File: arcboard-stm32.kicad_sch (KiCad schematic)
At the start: 85 parts, among them J10 Conn_01x04_Socket, J13 FFC05001-12SBA124W5M, J14 FFC05001-12SBA124W5M, J15 FFC05001-12SBA124W5M, J16 FFC05001-12SBA124W5M, J2 Conn_01x04_Socket, J3 FFC05001-12SBA124W5M, J4 FFC05001-12SBA124W5M, J5 Conn_01x02_Socket, J6 FFC05001-12SBA124W5M, J7 FFC05001-12SBA124W5M, J8 FFC05001-12SBA124W5M, J9 Conn_01x03_Socket, U1 XC6210B332MR-G, U10 1N4148W_C81598, U11 W25Q16JVSSIQTR, U12 TYPE-C-31-M-13, U13 2N7002, U15 TS-1187A-B-A-B, U2 TYPE-C-31-M-13, U3 STM32F405RGTx, U4 2N7002, U5 BAV70S,115, U6 BAV70S,115, U7 BAV70S,115, U8 BAV70S,115, U9 BAV70S,115, Y1 Crystal_GND24

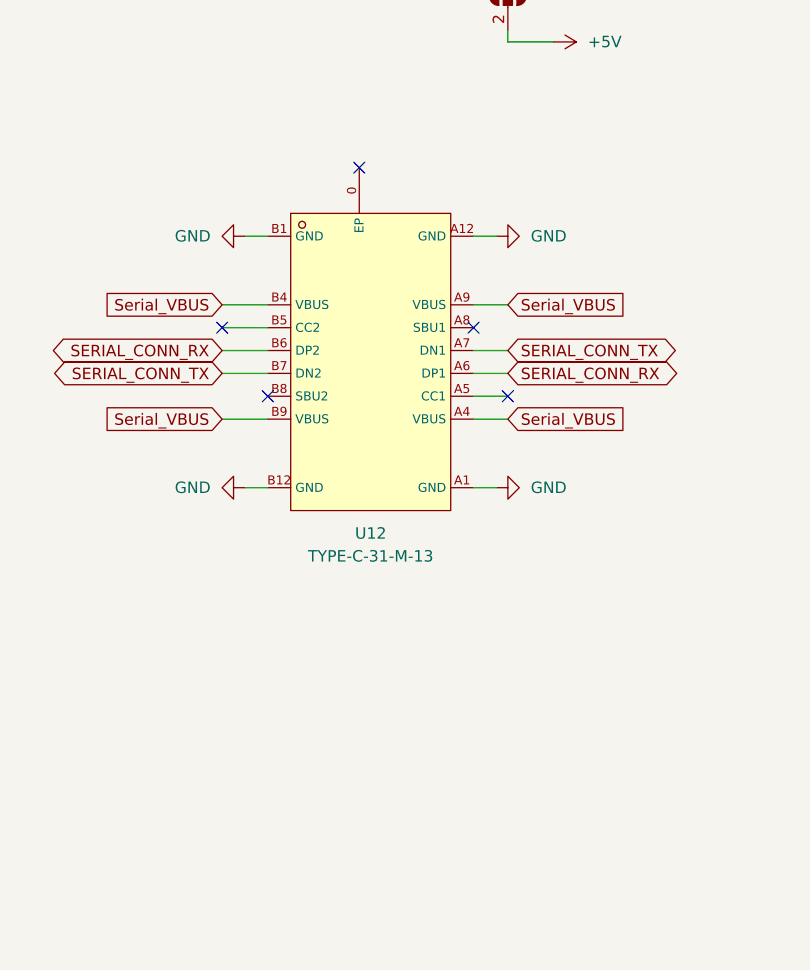
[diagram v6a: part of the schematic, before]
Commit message: moving to separate split connector, adding flash
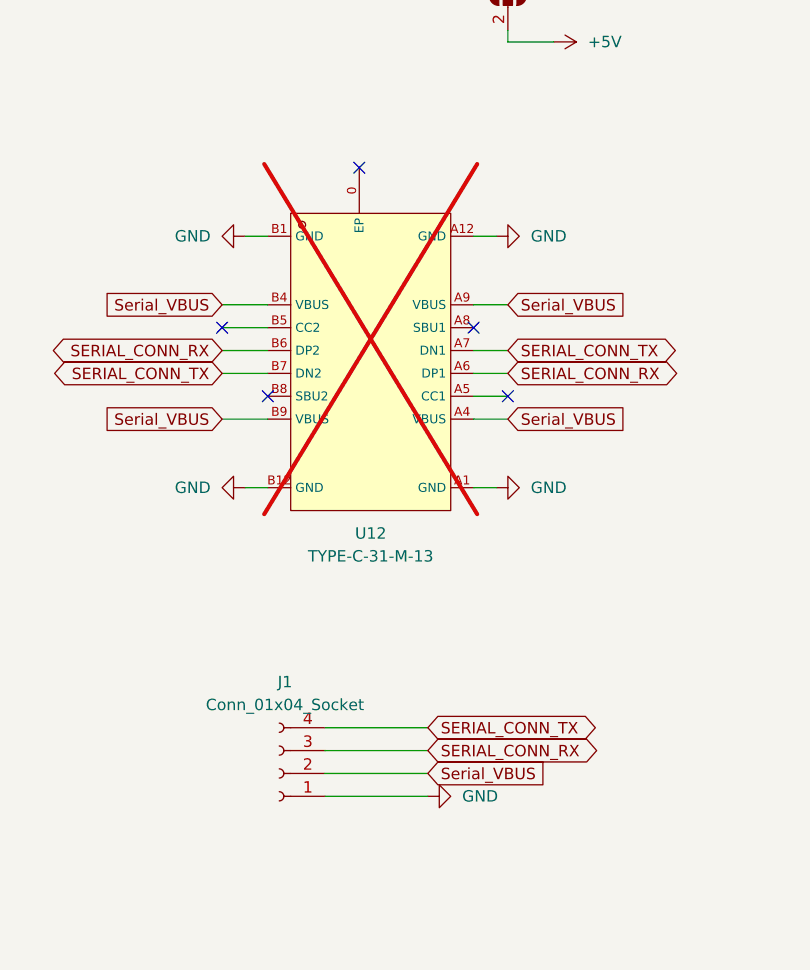
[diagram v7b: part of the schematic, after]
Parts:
- added J1: Conn_01x04_Socket, Connector_PinHeader_2.54mm:PinHeader_1x04_P2.54mm_Vertical, symbol Connector:Conn_01x04_Socket
- U12: now not fitted; now left out of the parts list
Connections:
- net GND: now also J1.1 (Pin_1)
- net SERIAL_CONN_RX: now also J1.3 (Pin_3)
- net SERIAL_CONN_TX: now also J1.4 (Pin_4)
- net Serial_VBUS: now also J1.2 (Pin_2)
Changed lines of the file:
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@@
 	(wire
 		(pts
+			(xy 647.7 458.47) (xy 659.13 458.47)
+		)
+		(stroke
+			(width 0)
+			(type default)
+		)
+	)
+	(wire
+		(pts
 			(xy 424.18 223.52) (xy 424.18 219.71)
 		)
@@
 	(wire
 		(pts
+			(xy 647.7 461.01) (xy 659.13 461.01)
+		)
+		(stroke
+			(width 0)
+			(type default)
+		)
+	)
+	(wire
+		(pts
 			(xy 294.64 490.22) (xy 298.45 490.22)
 		)
@@
 	(wire
 		(pts
+			(xy 647.7 455.93) (xy 659.13 455.93)
+		)
+		(stroke
+			(width 0)
+			(type default)
+		)
+	)
+	(wire
+		(pts
 			(xy 480.06 307.34) (xy 468.63 307.34)
 		)
@@
 	(wire
 		(pts
+			(xy 647.7 453.39) (xy 659.13 453.39)
+		)
+		(stroke
+			(width 0)
+			(type default)
+		)
+	)
+	(wire
+		(pts
 			(xy 101.6 227.33) (xy 104.14 227.33)
 		)
@@
 		)
 	)
+	(global_label "Serial_VBUS"
+		(shape input)
+		(at 659.13 458.47 0)
+		(fields_autoplaced yes)
+		(effects
+			(font
+				(size 1.27 1.27)
+			)
+			(justify left)
+		)
+		(property "Intersheetrefs" "${INTERSHEET_REFS}"
+			(at 673.4847 458.47 0)
+			(effects
+				(font
+					(size 1.27 1.27)
+				)
+				(justify left)
+				(hide yes)
+			)
+		)
+	)
 	(global_label "ENCODER1_R2"
 		(shape input)
@@
 		)
 	)
+	(global_label "SERIAL_CONN_TX"
+		(shape bidirectional)
+		(at 659.13 453.39 0)
+		(fields_autoplaced yes)
+		(effects
+			(font
+				(size 1.27 1.27)
+			)
+			(justify left)
+		)
+		(property "Intersheetrefs" "${INTERSHEET_REFS}"
+			(at 678.9503 453.39 0)
+			(effects
+				(font
+					(size 1.27 1.27)
+				)
+				(justify left)
+				(hide yes)
+			)
+		)
+	)
 	(global_label "ROW0"
 		(shape input)
@@
 		)
 	)
+	(global_label "SERIAL_CONN_RX"
+		(shape bidirectional)
+		(at 659.13 455.93 0)
+		(fields_autoplaced yes)
+		(effects
+			(font
+				(size 1.27 1.27)
+			)
+			(justify left)
+		)
+		(property "Intersheetrefs" "${INTERSHEET_REFS}"
+			(at 679.2527 455.93 0)
+			(effects
+				(font
+					(size 1.27 1.27)
+				)
+				(justify left)
+				(hide yes)
+			)
+		)
+	)
 	(global_label "LCD_DC"
 		(shape input)
@@
 	)
 	(symbol
+		(lib_id "power:GND")
+		(at 659.13 461.01 90)
+		(unit 1)
+		(exclude_from_sim no)
+		(in_bom yes)
+		(on_board yes)
+		(dnp no)
+		(fields_autoplaced yes)
+		(property "Reference" "#PWR091"
+			(at 665.48 461.01 0)
+			(effects
+				(font
+					(size 1.27 1.27)
+				)
+				(hide yes)
+			)
+		)
+		(property "Value" "GND"
+			(at 662.94 461.0099 90)
+			(effects
+				(font
+					(size 1.27 1.27)
+				)
+				(justify right)
+			)
+		)
+		(property "Footprint" ""
+			(at 659.13 461.01 0)
+			(effects
+				(font
+					(size 1.27 1.27)
+				)
+				(hide yes)
+			)
+		)
+		(property "Datasheet" ""
+			(at 659.13 461.01 0)
+			(effects
+				(font
+					(size 1.27 1.27)
+				)
+				(hide yes)
+			)
+		)
+		(property "Description" ""
+			(at 659.13 461.01 0)
+			(effects
+				(font
+					(size 1.27 1.27)
+				)
+			)
+		)
+		(pin "1"
+		)
+		(instances
+			(project "arcboard-stm32"
+				(path "/77409937-8008-4619-ae71-6a56c8773006"
+					(reference "#PWR091")
+					(unit 1)
+				)
+			)
+		)
+	)
+	(symbol
 		(lib_id "Device:C_Small")
 		(at 421.64 358.14 180)
@@
 		(at 654.05 408.94 0)
 		(unit 1)
-		(exclude_from_sim no)
-		(in_bom yes)
-		(on_board yes)
-		(dnp no)
+		(exclude_from_sim yes)
+		(in_bom no)
+		(on_board no)
+		(dnp yes)
 		(fields_autoplaced yes)
 		(property "Reference" "U12"
@@
 					(unit 1)
 				)
+			)
+		)
+	)
+	(symbol
+		(lib_id "Connector:Conn_01x04_Socket")
+		(at 642.62 458.47 180)
+		(unit 1)
+		(exclude_from_sim no)
+		(in_bom yes)
+		(on_board yes)
+		(dnp no)
+		(fields_autoplaced yes)
+		(property "Reference" "J1"
+			(at 643.255 448.31 0)
+			(effects
+				(font
+					(size 1.27 1.27)
+				)
+			)
+		)
+		(property "Value" "Conn_01x04_Socket"
+			(at 643.255 450.85 0)
+			(effects
+				(font
+					(size 1.27 1.27)
+				)
+			)
+		)
+		(property "Footprint" "Connector_PinHeader_2.54mm:PinHeader_1x04_P2.54mm_Vertical"
+			(at 642.62 458.47 0)
+			(effects
+				(font
+					(size 1.27 1.27)
+				)
+				(hide yes)
+			)
+		)
+		(property "Datasheet" "~"
+			(at 642.62 458.47 0)
+			(effects
+				(font
+					(size 1.27 1.27)
+				)
+				(hide yes)
+			)
+		)
+		(property "Description" "Generic connector, single row, 01x04, script generated"
+			(at 642.62 458.47 0)
+			(effects
+				(font
+					(size 1.27 1.27)
+				)
+				(hide yes)
+			)
+		)
+		(pin "1"
+		)
+		(pin "2"
+		)
+		(pin "4"
+		)
+		(pin "3"
+		)
+		(instances
+			(project ""
+				(path "/77409937-8008-4619-ae71-6a56c8773006"
+					(reference "J1")
+					(unit 1)
+				)

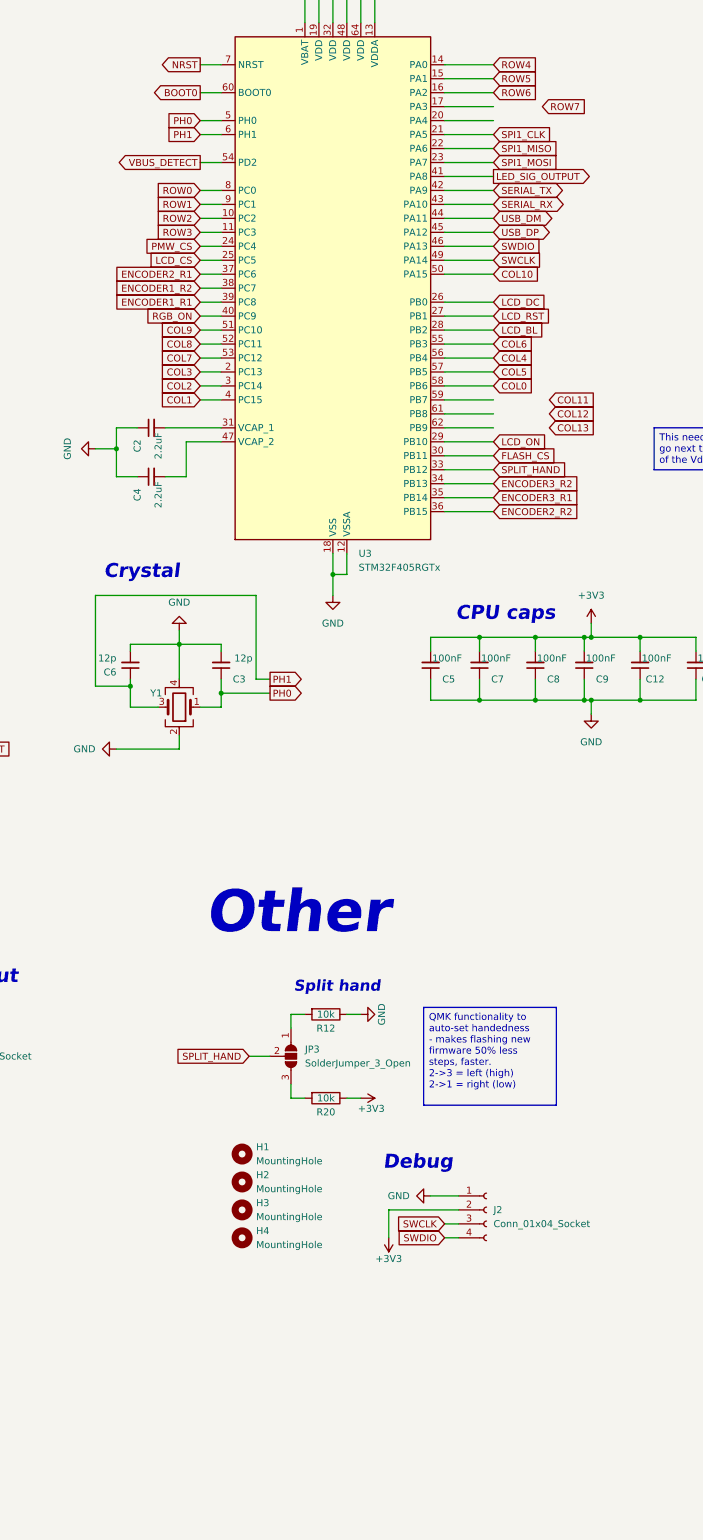
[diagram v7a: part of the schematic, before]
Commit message: adding spare pins, more routing
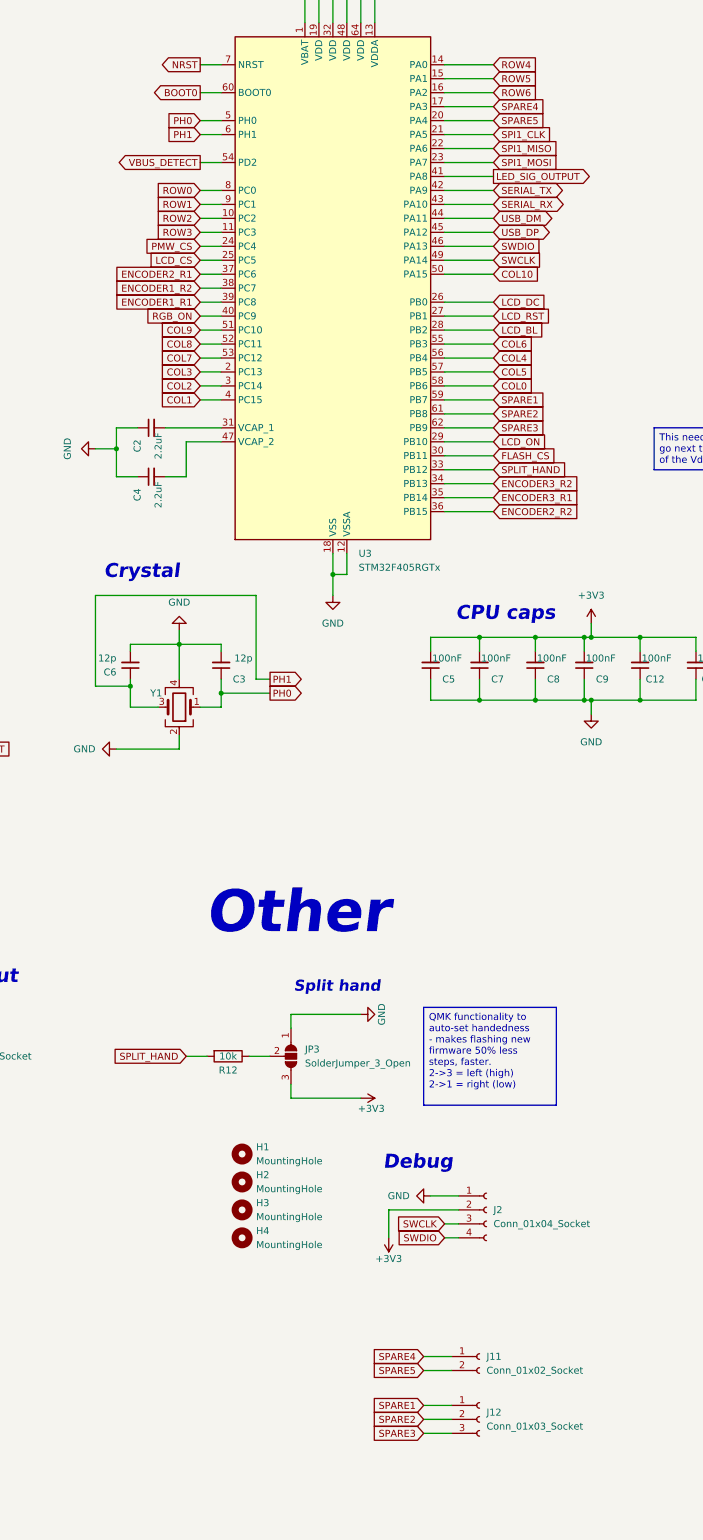
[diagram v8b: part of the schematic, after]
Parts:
- removed R20: 10k, Resistor_SMD:R_0402_1005Metric, symbol Device:R
- added J11: Conn_01x02_Socket, Connector_PinHeader_1.00mm:PinHeader_1x02_P1.00mm_Vertical, symbol Connector:Conn_01x02_Socket
- added J12: Conn_01x03_Socket, Connector_PinHeader_1.00mm:PinHeader_1x03_P1.00mm_Vertical, symbol Connector:Conn_01x03_Socket
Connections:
- net +3V3: now also JP3.3 (B)
- net GND: now also JP3.1 (A); no longer R12.1
- net SPLIT_HAND: now also R12.2; no longer JP3.2 (C)
- net SPARE4: now reaches U3.17 (PA3)
- net SPARE4: now also J11.1 (Pin_1)
- net SPARE5: now reaches U3.20 (PA4)
- net SPARE5: now also J11.2 (Pin_2)
- net SPARE1: now reaches U3.59 (PB7)
- net SPARE1: now also J12.1 (Pin_1)
- net SPARE2: now reaches U3.61 (PB8)
- net SPARE2: now also J12.2 (Pin_2)
- net SPARE3: now reaches U3.62 (PB9)
- net SPARE3: now also J12.3 (Pin_3)
- new net: JP3.2 (C), R12.1
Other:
- moved on the sheet: R12
